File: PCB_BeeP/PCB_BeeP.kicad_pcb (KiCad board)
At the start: 2 copper layers, 109.2 x 63.5 mm, 18 parts, among them J1 Conn_01x02, J2 Conn_01x04, J3 Conn_01x02, J4 Conn_01x02, J5 Conn_01x04, J6 Conn_01x04, J7 Conn_01x02, U1 LM7805_TO220, U2 TP4056, U3 LM7805_TO220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

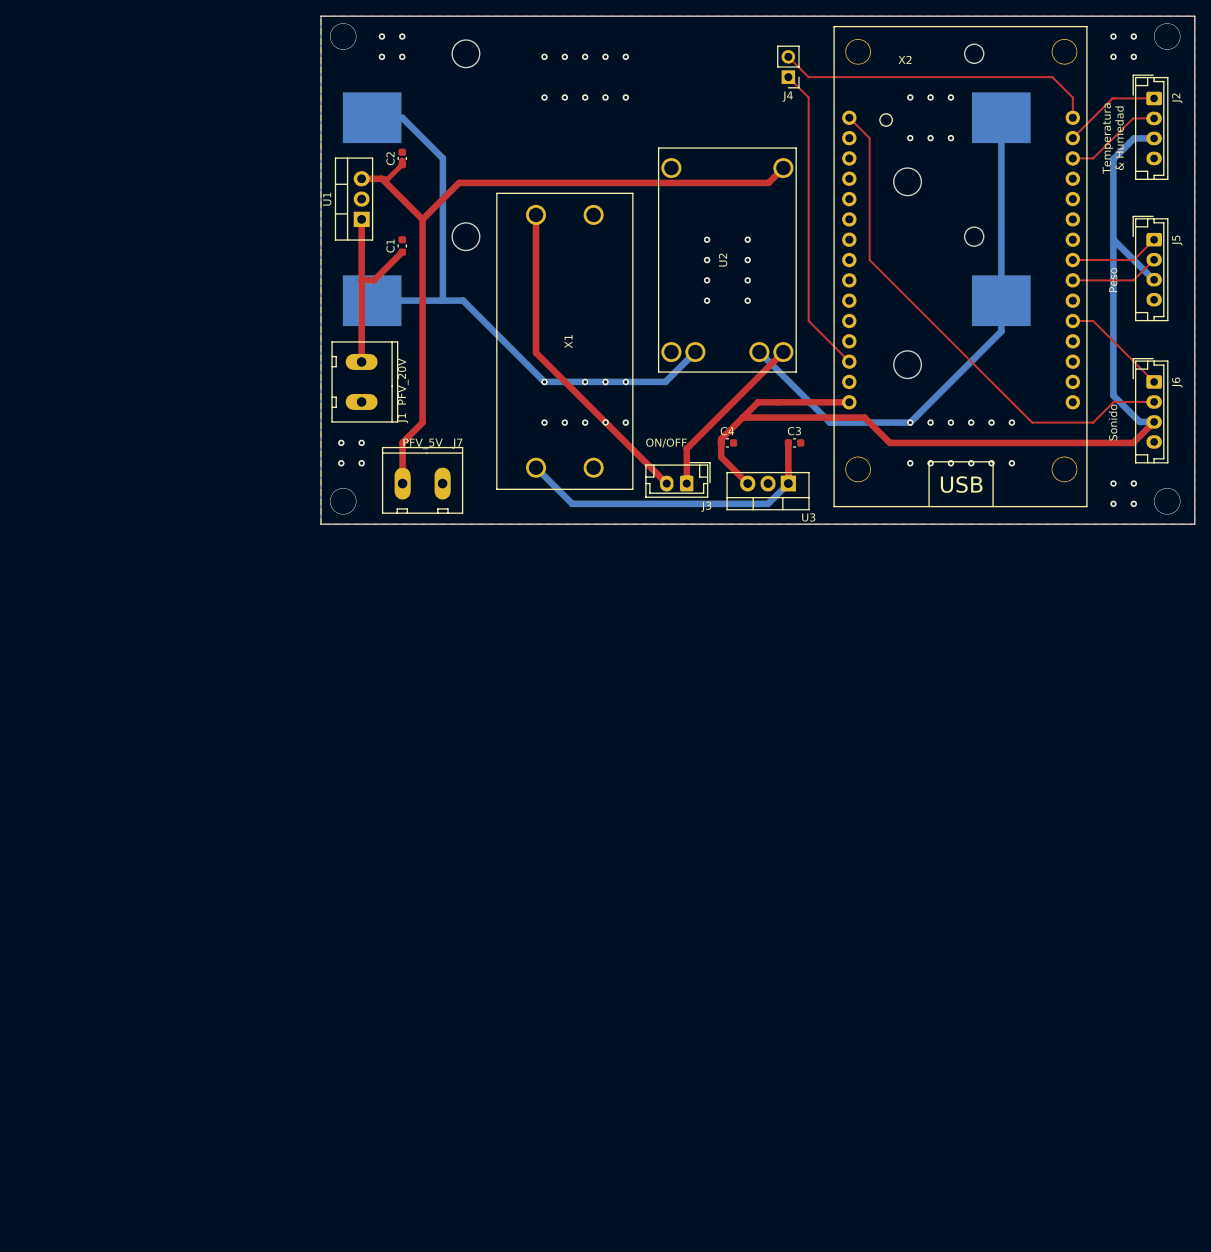
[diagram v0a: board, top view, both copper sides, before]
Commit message: Placa abejas final - Isi
Agregados conectores porsiaca (GPS y 3G), pin de monitoreo de carga de la batería y modificación al lado de potencia (se asume que se tendrá para entonces un regulador MPPT para el panel FV, modificación a Julio Charger).
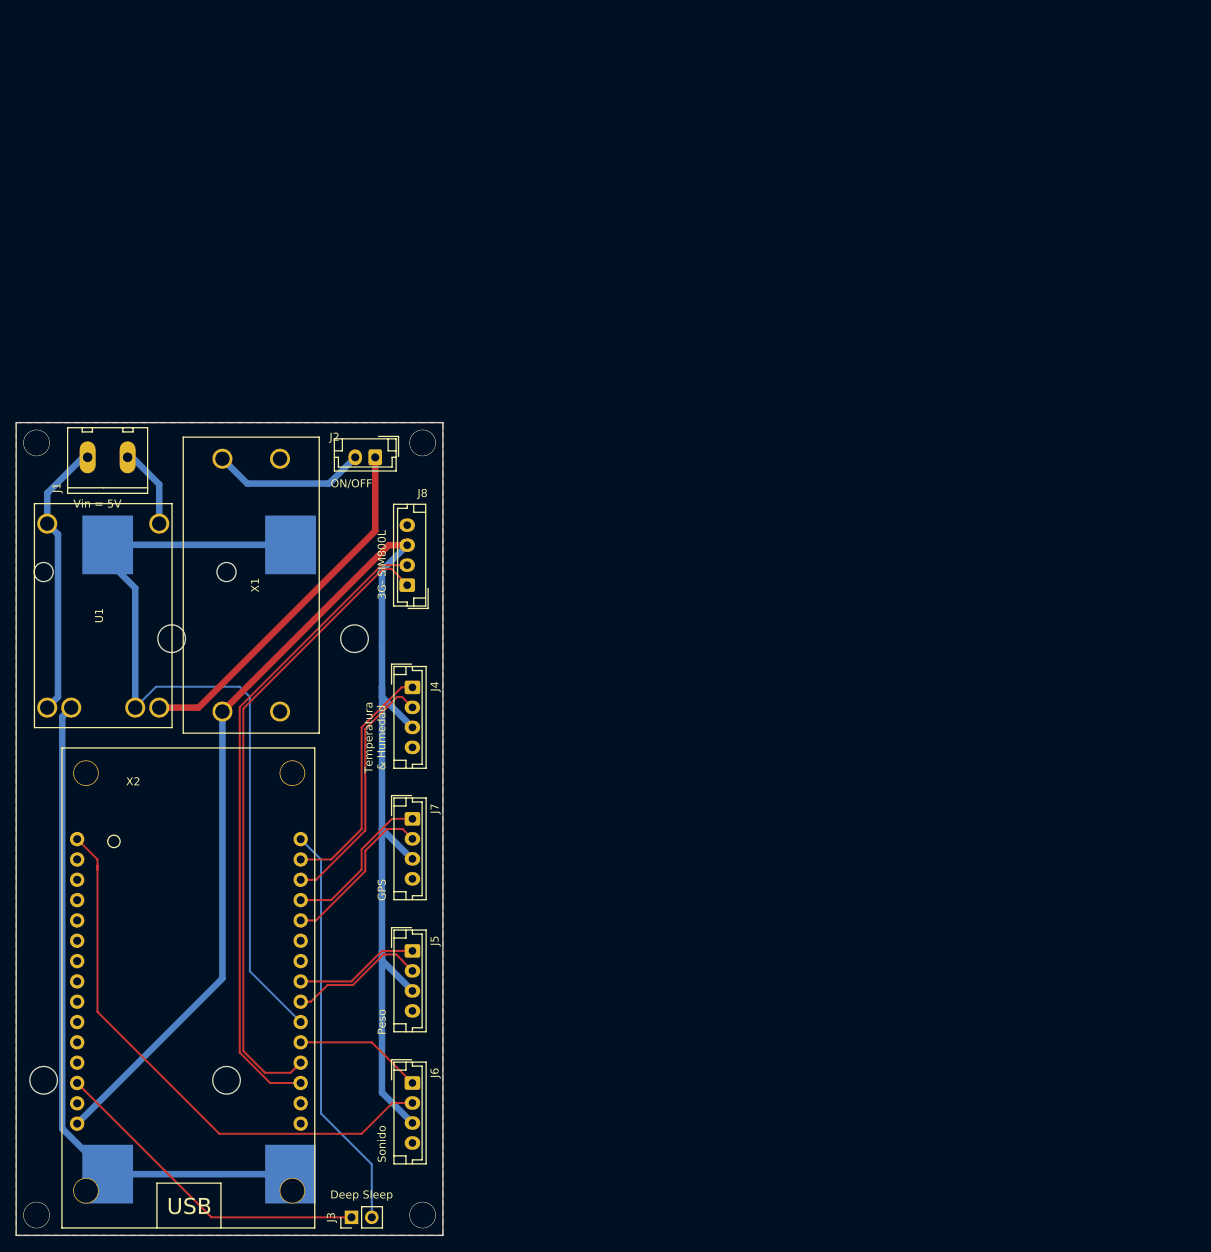
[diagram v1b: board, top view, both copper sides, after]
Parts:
- removed C1, C2, C3, C4: CP, Capacitor_SMD:C_0603_1608Metric
- removed the J1 at (114.3, 68.6)
- removed the U1 at (114.3, 48.3)
- removed U3: LM7805_TO220, Package_TO_SOT_THT:TO-220-3_Vertical
- added J7: Conn_01x04, Connector_JST:JST_EH_B4B-EH-A_1x04_P2.50mm_Vertical, F.Cu at (120.7, 123.2)
- added J8: Conn_01x04, Connector_JST:JST_EH_B4B-EH-A_1x04_P2.50mm_Vertical, F.Cu at (120.0, 94.0)
- moved J3 152.6 mm to (113.0, 173.0), turned to 90 degrees
- moved X2 132.1 mm to (78.7, 125.7)
- moved J5 128.4 mm to (120.7, 139.7)
- moved J6 127.6 mm to (120.7, 156.2)
- moved J4 118.4 mm to (120.7, 106.8)
- moved BT2 117.6 mm to (82.5, 128.3), turned to 270 degrees
- moved U1 89.8 mm to (82.0, 97.8)
- moved BT1 85.6 mm to (105.4, 128.3), turned to 270 degrees
- moved X1 49.7 mm to (100.5, 94.0)
- moved J1 39.5 mm to (82.5, 78.0), turned to 0 degrees
- moved J2 39.1 mm to (116.0, 78.0)
- renumbered J7 to J1, J3 to J2, J4 to J3, J2 to J4, U2 to U1
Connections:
- net /PFV+_5V renamed /PFV-5V
- X1 pad 4: Net-(C3-Pad1) -> /5V
- X2 pad 21: Net-(X2-Pad21) -> Net-(BT1-Pad1)
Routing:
- net /PFV-5V: track 95.3 -> 10.3 mm
- net Net-(J8-Pad1): track 0.00 -> 81.3 mm
- net Net-(J8-Pad2): track 0.00 -> 80.7 mm
- net Net-(C3-Pad1): track 41.4 -> 0.00 mm
- net Net-(BT1-Pad1): track 66.0 -> 103.8 mm, vias 1 -> 0
- net GND: track 0.00 -> 34.8 mm, vias 59 -> 4
- net /5V: track 155.8 -> 184.5 mm
- net /PFV+_20V: track 24.4 -> 0.00 mm
- net Net-(J2-Pad1): track 21.4 -> 45.3 mm
- net Net-(J2-Pad2): track 40.3 -> 19.2 mm, vias 1 -> 0
- net Net-(J7-Pad2): track 0.00 -> 20.7 mm
- net Net-(J7-Pad1): track 0.00 -> 19.7 mm
- net Net-(J4-Pad2): track 12.2 -> 31.8 mm
- net Net-(J4-Pad1): track 12.2 -> 30.3 mm
- net Net-(J3-Pad2): track 40.2 -> 51.0 mm
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- added copper zone on B.Cu, net GND
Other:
- board size 109.2 x 63.5 mm -> 53.3 x 101.6 mm
- board text added: "3G- SIM800L"
- board text added: "Deep Sleep"
- board text added: "GPS"
- board text added: "Vin = 5V"
- board text removed: "PFV_20V"
- board text removed: "PFV_5V"
